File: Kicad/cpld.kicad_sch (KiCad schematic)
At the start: 16 parts, among them J2 Conn_01x06_Pin, U15 AMS1117-3.3, U16 XC95144XL-TQ144

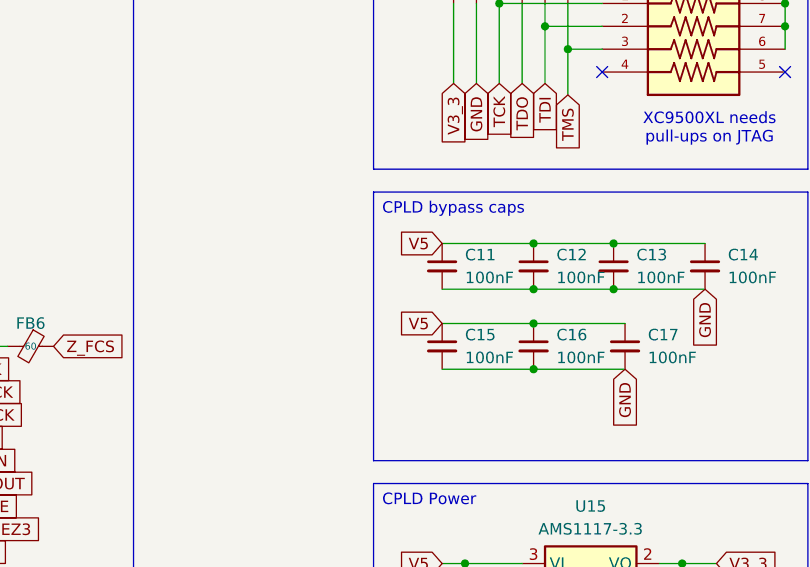
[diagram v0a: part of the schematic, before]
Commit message: CPLD bypass caps need to be on the 3.3V rail, not 5V
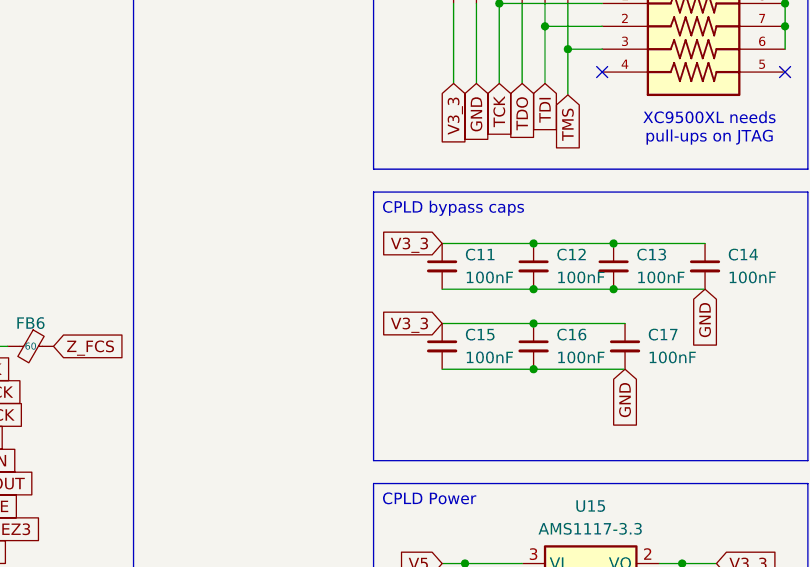
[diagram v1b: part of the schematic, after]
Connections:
- net V3_3: now also C11.1, C12.1, C13.1, C14.1, C15.1, C16.1, C17.1
- net V5: no longer C11.1, C12.1, C13.1, C14.1, C15.1, C16.1, C17.1

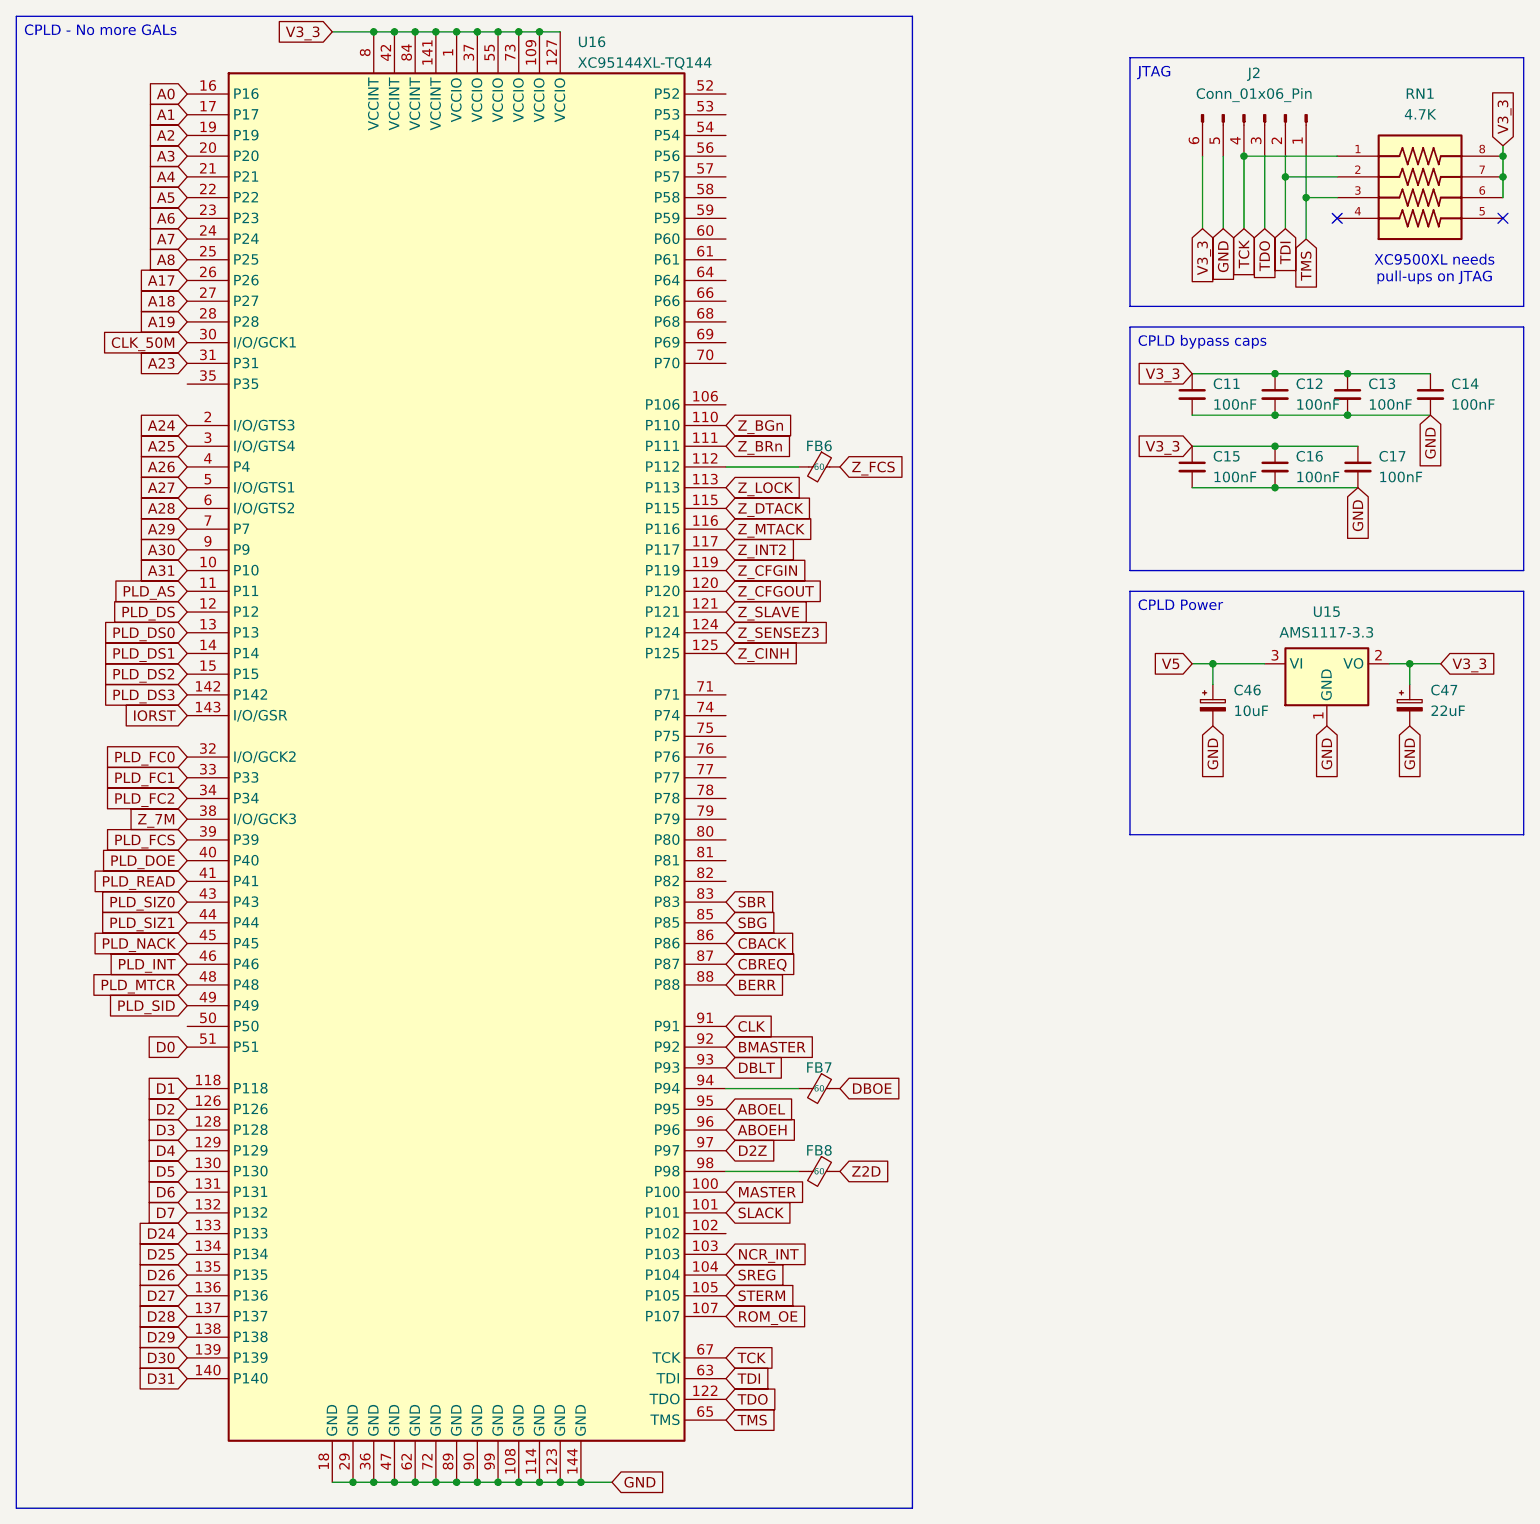
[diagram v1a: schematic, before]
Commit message: CPLD fixes
* Terminate unused CPLD connections with NC
* Move D0 to pin 117 to line up with the other databus pins
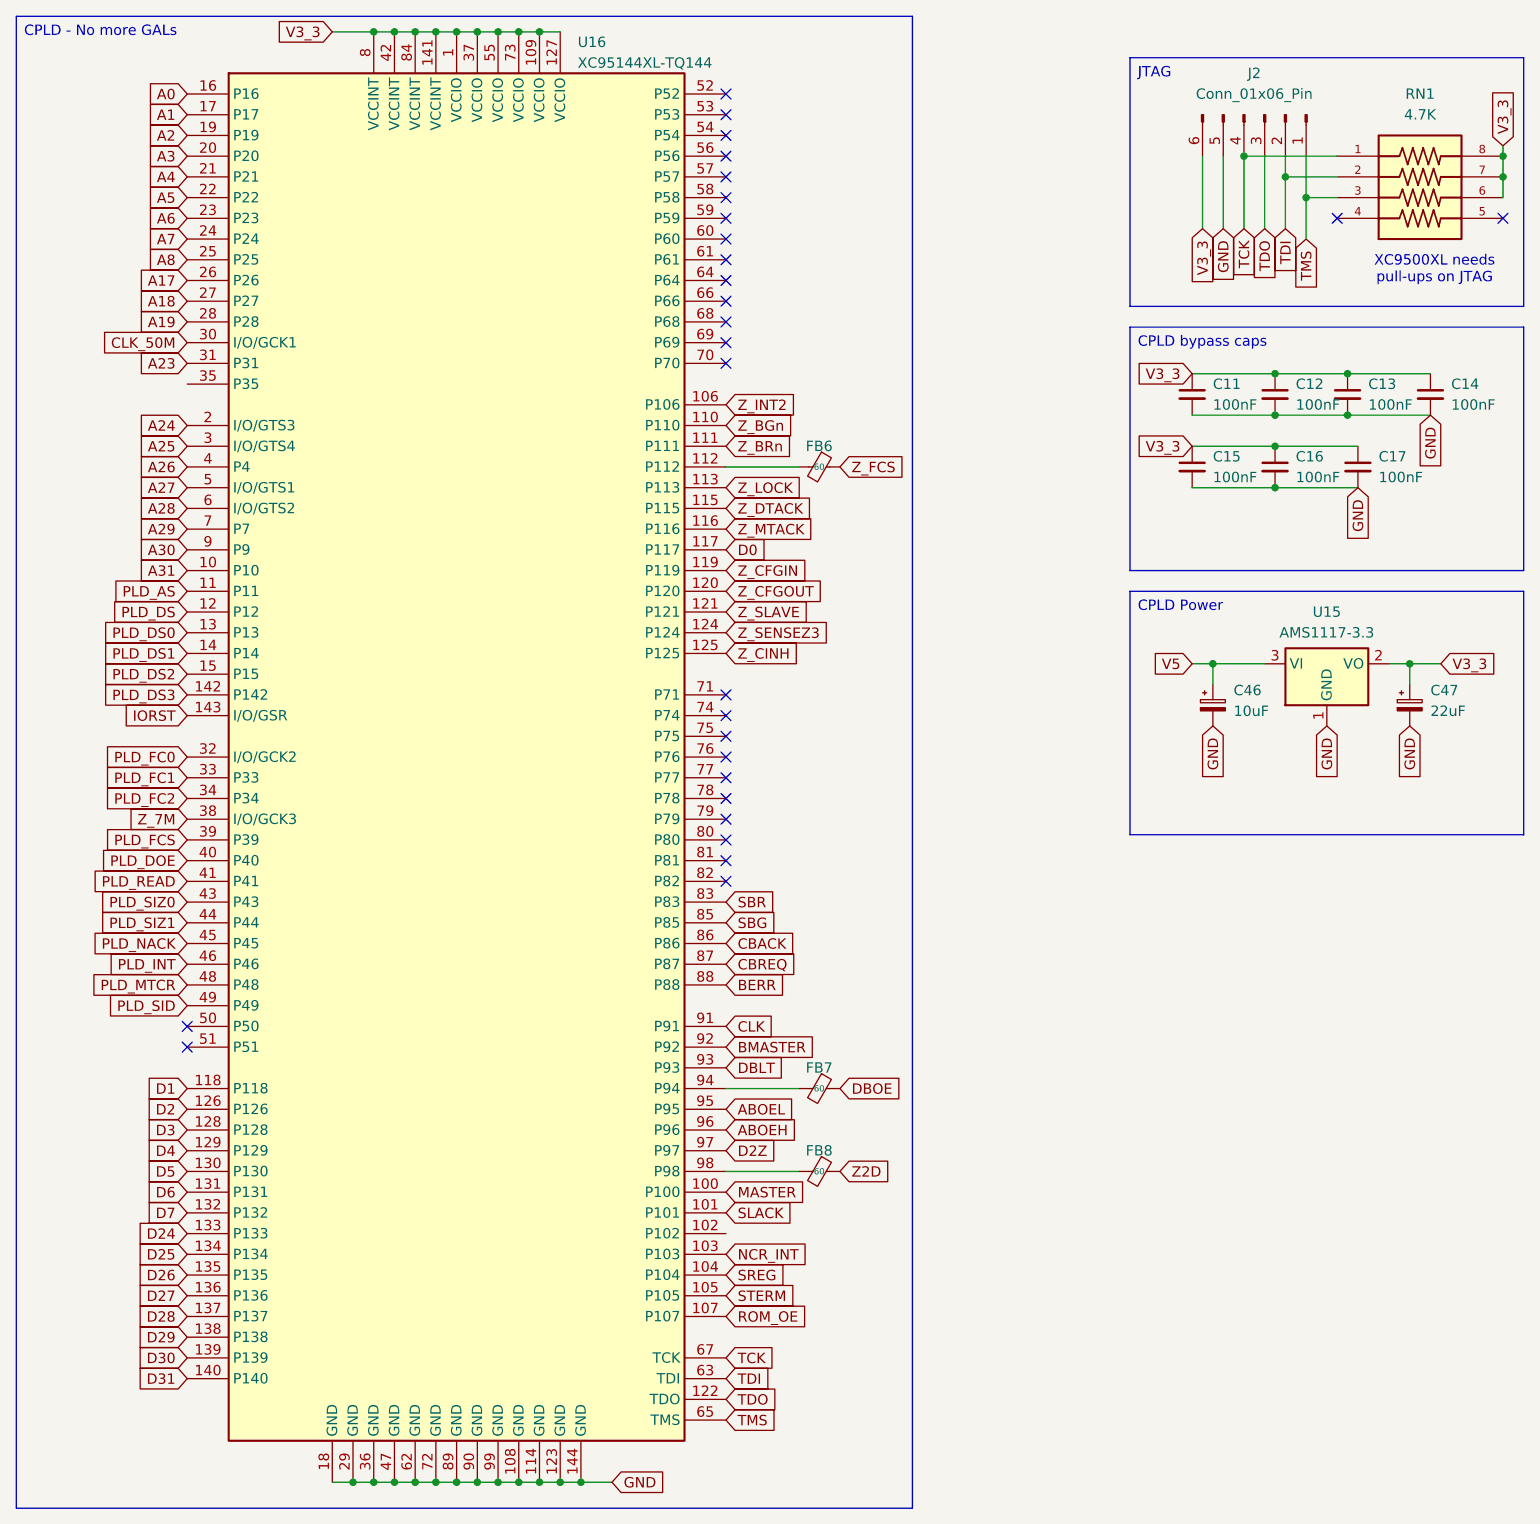
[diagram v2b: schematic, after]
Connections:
- net D0: now also U16.117 (P117); no longer U16.51 (P51)
- net Z_INT2: now also U16.106 (P106); no longer U16.117 (P117)
- no-connect marks 2 -> 28

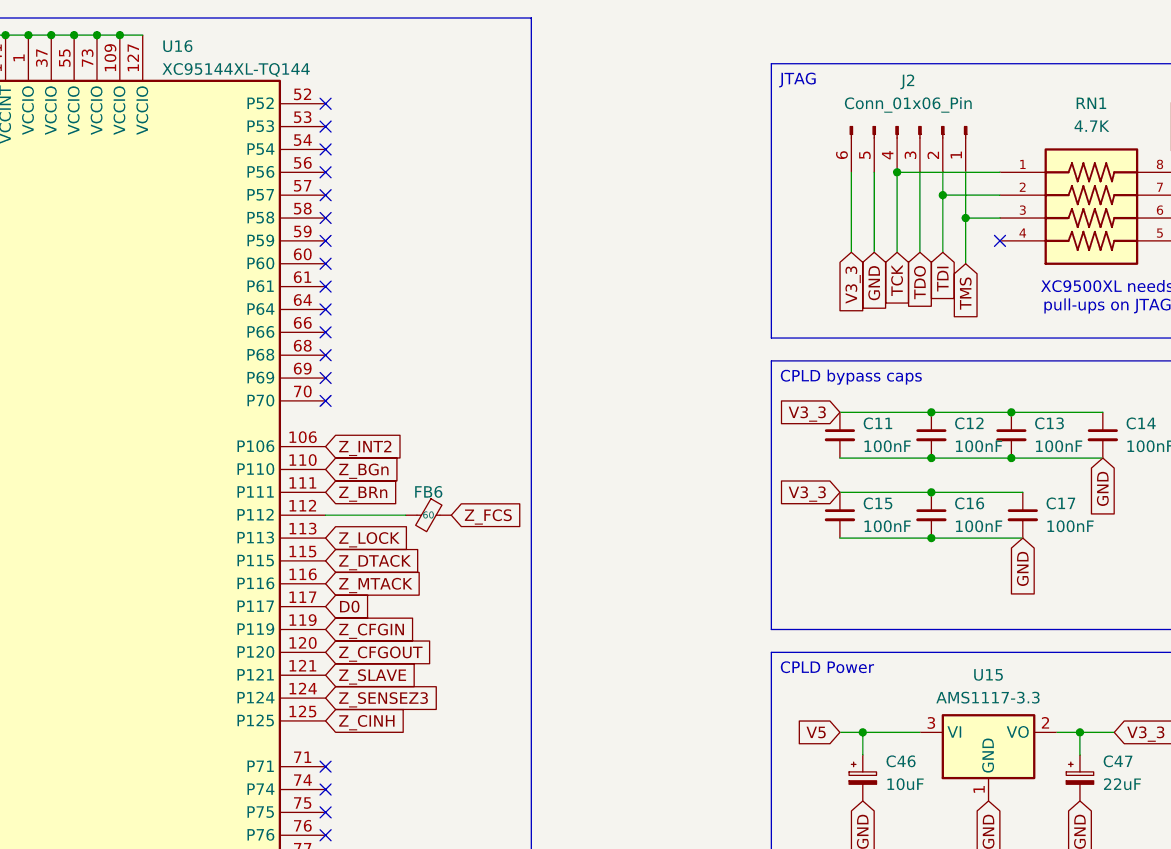
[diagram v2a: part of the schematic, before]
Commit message: Rename all Uxx parts from U1 to U13 for consistency
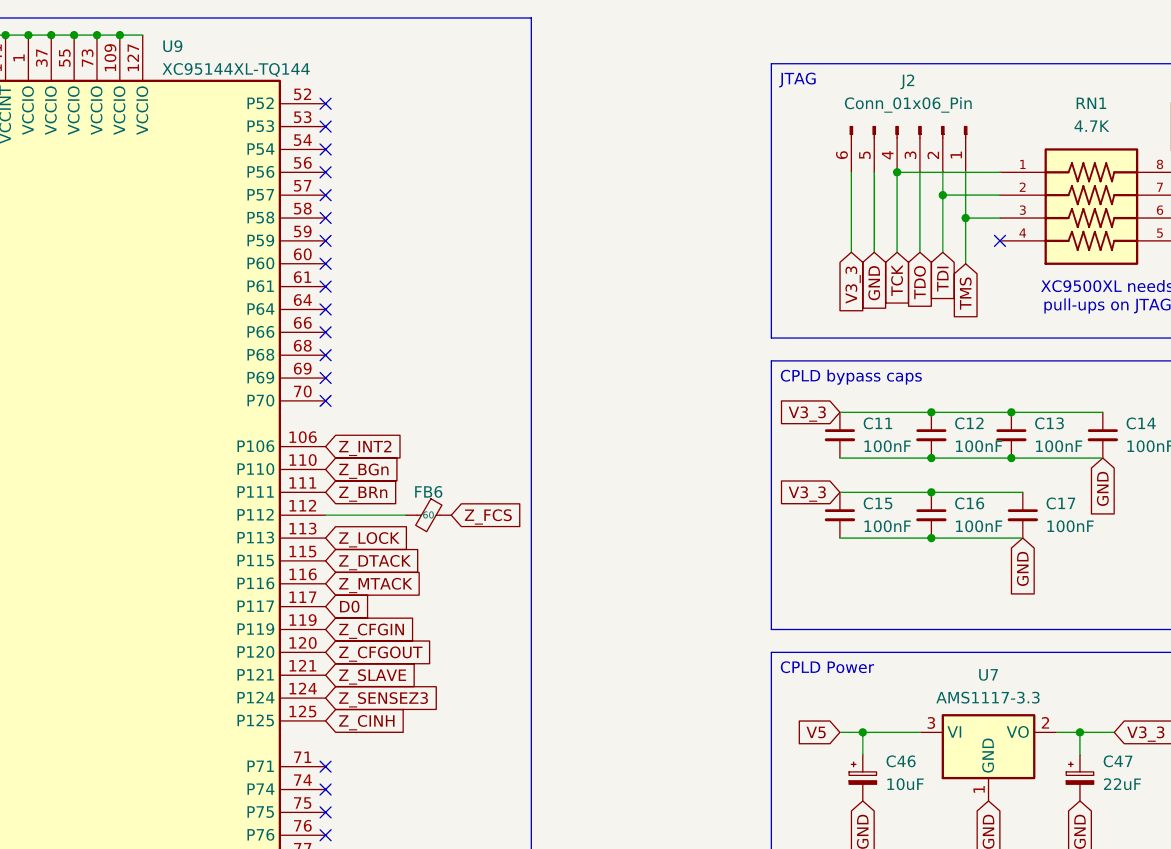
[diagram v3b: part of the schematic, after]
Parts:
- renumbered U15 to U7, U16 to U9
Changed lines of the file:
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@@
 		(dnp no)
 		(fields_autoplaced yes)
-		(property "Reference" "U16"
+		(property "Reference" "U9"
 			(at 82.1533 16.51 0)
 			(effects
@@
 			(project ""
 				(path "/8f9f4021-47aa-41d9-bea7-f6ccf72098bb/6ae4417c-9681-4757-b289-033d6e31deb3"
-					(reference "U16")
+					(reference "U9")
 					(unit 1)
 				)
@@
 		(dnp no)
 		(fields_autoplaced yes)
-		(property "Reference" "U15"
+		(property "Reference" "U7"
 			(at 173.99 86.36 0)
 			(effects
@@
 			(project ""
 				(path "/8f9f4021-47aa-41d9-bea7-f6ccf72098bb/6ae4417c-9681-4757-b289-033d6e31deb3"
-					(reference "U15")
-					(unit 1)
-				)
+					(reference "U7")
+					(unit 1)
+				)

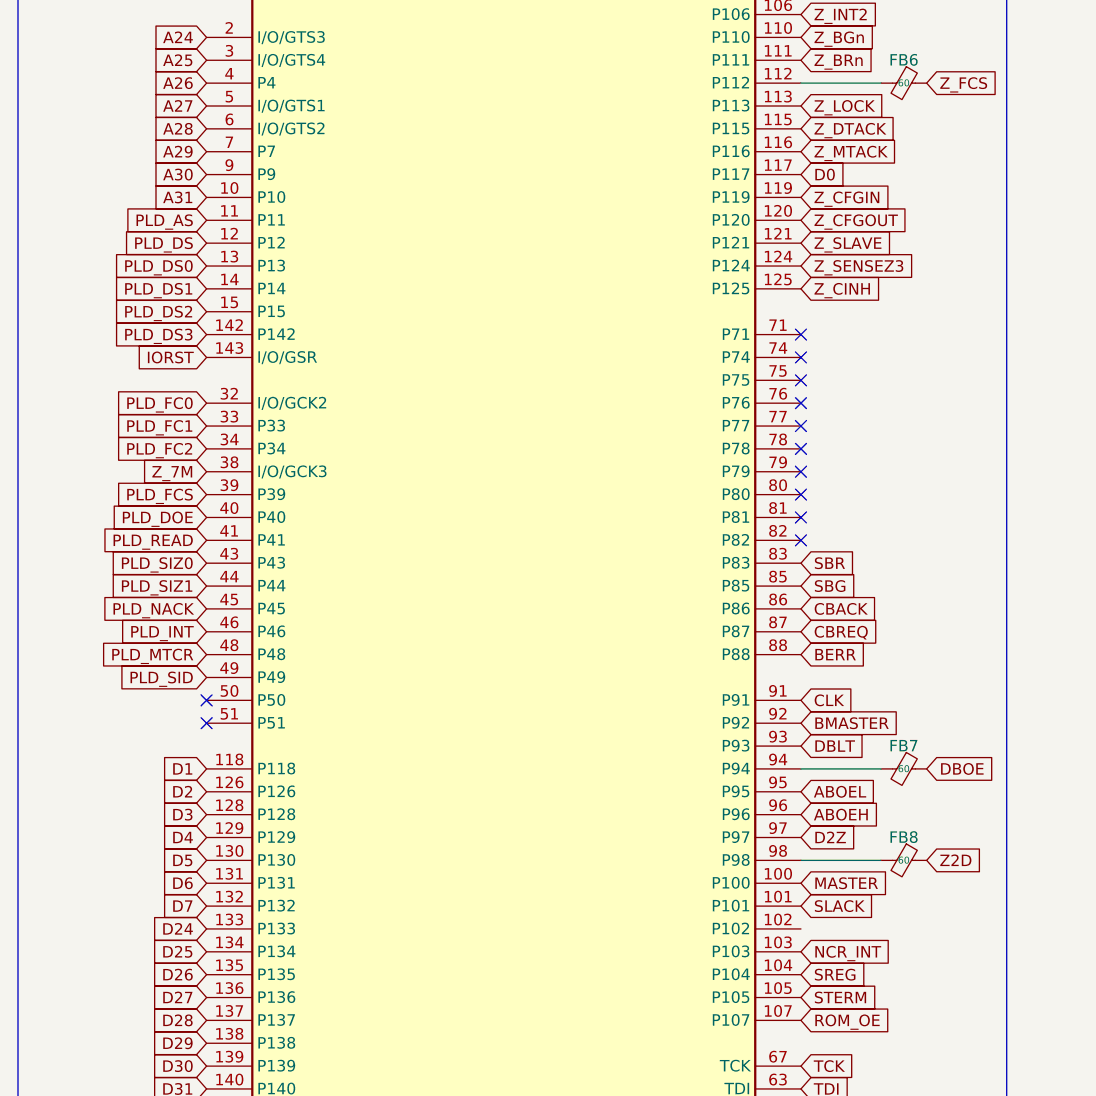
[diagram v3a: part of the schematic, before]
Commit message: Move D0/D1 (again) and remove PLD_INT
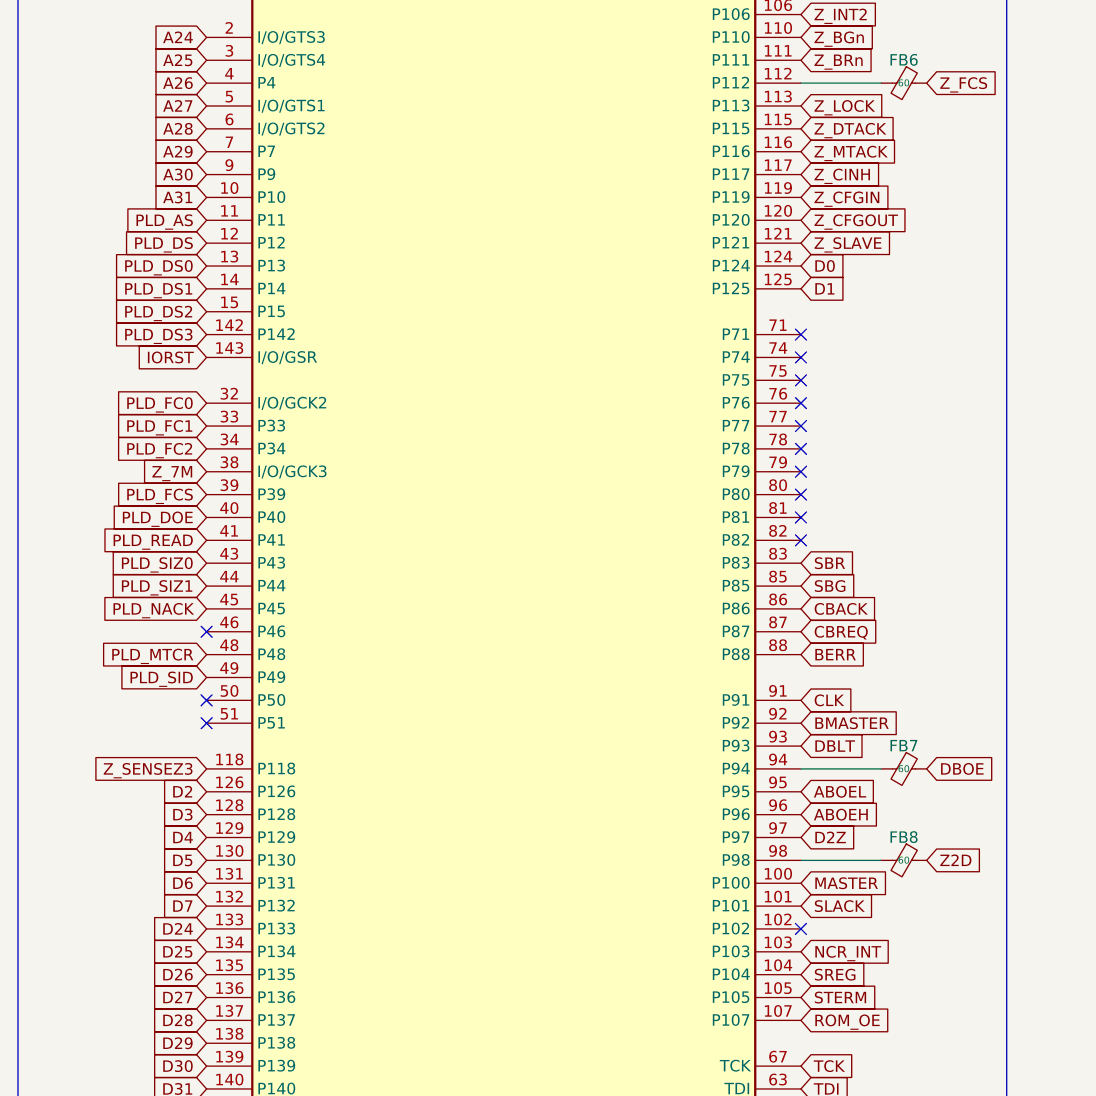
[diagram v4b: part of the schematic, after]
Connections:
- net D0: now also U9.124 (P124); no longer U9.117 (P117)
- net D1: now also U9.125 (P125); no longer U9.118 (P118)
- net Z_CINH: now also U9.117 (P117); no longer U9.125 (P125)
- net Z_SENSEZ3: now also U9.118 (P118); no longer U9.124 (P124)
- net PLD_INT: no longer names the net of U9.46 (P46)
- no-connect marks 28 -> 30
